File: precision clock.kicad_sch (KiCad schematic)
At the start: 45 parts, among them J1 JACK, Q1 2N5401, Q2 2N5401

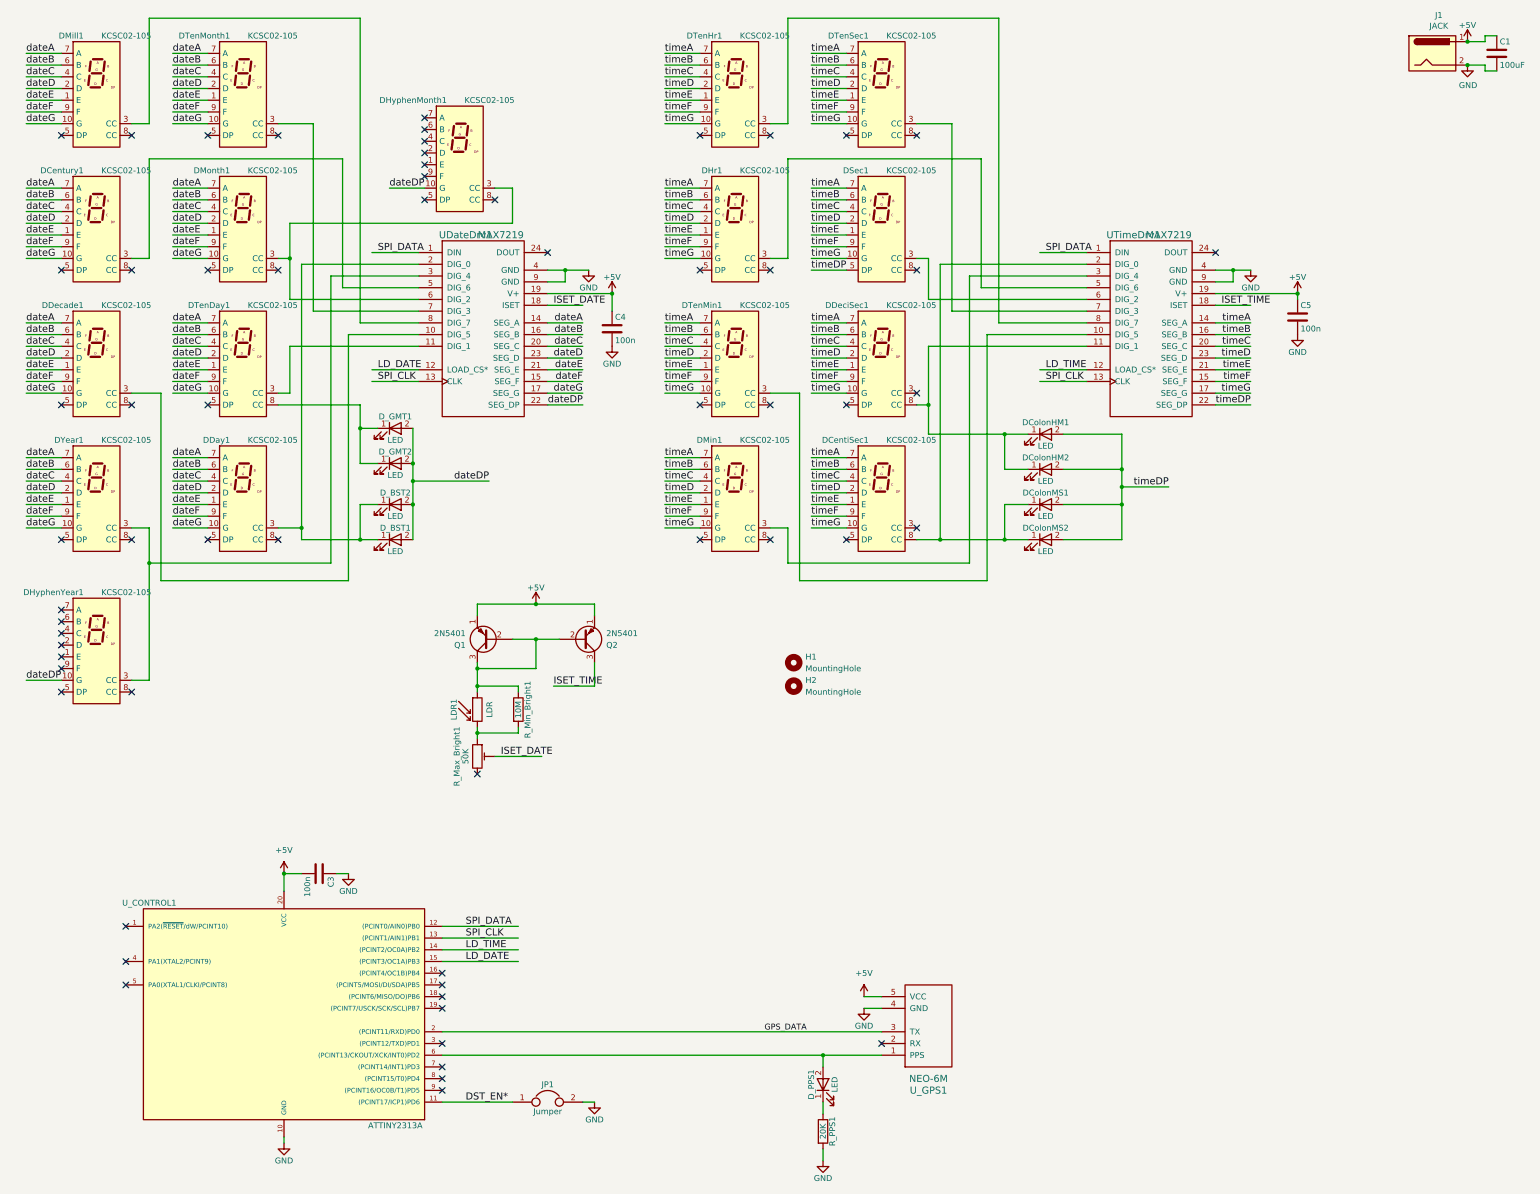
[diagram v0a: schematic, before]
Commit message: Add jumpers for permaDST and UTC
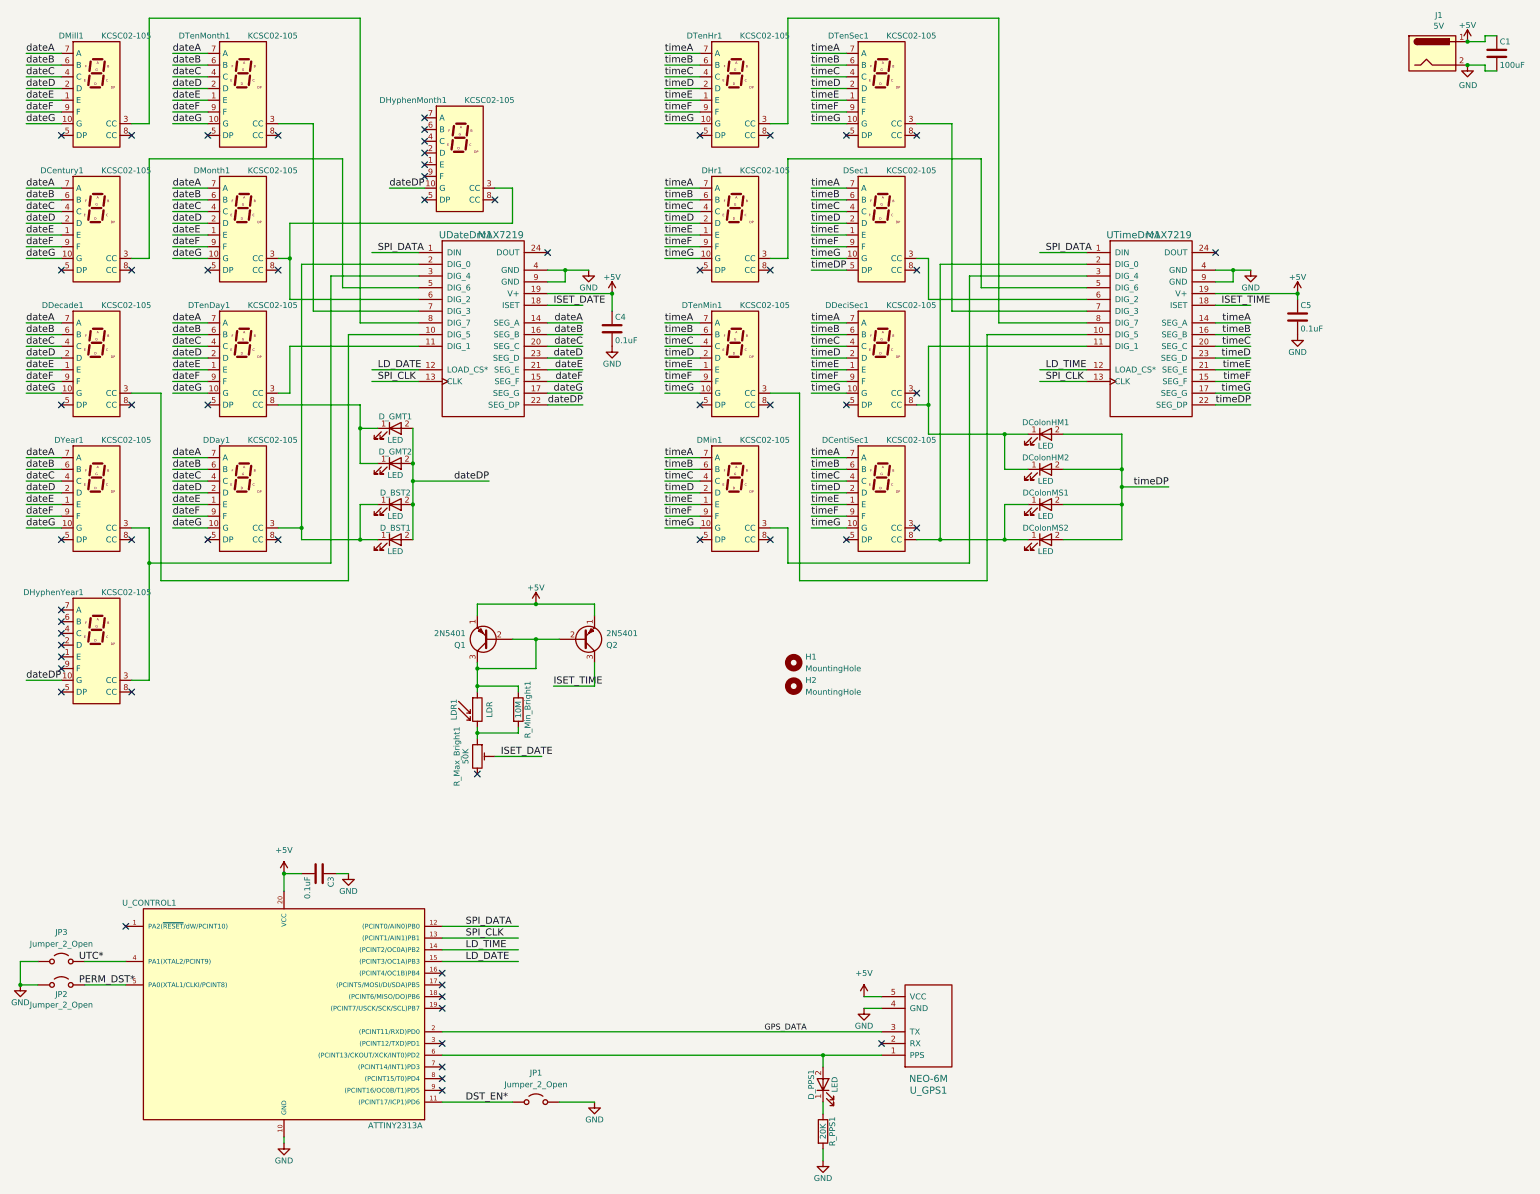
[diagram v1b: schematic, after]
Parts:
- removed JP1: Jumper, Connector_PinHeader_2.54mm:PinHeader_1x02_P2.54mm_Vertical, symbol precision-clock-rescue:Jumper
- added JP1, JP2, JP3: Jumper_2_Open, Connector_PinHeader_2.54mm:PinHeader_1x02_P2.54mm_Vertical, symbol Jumper:Jumper_2_Open
- C3, C4, C5: value 100n -> 0.1uF
- J1: value JACK -> 5V; footprint precision clock:BarrelJack_2 -> Connector_BarrelJack:BarrelJack_Horizontal
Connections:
- net DST_EN*: now also JP1.1 (A)
- net GND: now also JP1.2 (B), JP2.2 (B), JP3.2 (B)
- net at U_CONTROL1.4 (PA1(XTAL2/PCINT9)): now also JP3.1 (A)
- net at U_CONTROL1.5 (PA0(XTAL1/CLKI/PCINT8)): now also JP2.1 (A)
- no-connect marks 61 -> 59
